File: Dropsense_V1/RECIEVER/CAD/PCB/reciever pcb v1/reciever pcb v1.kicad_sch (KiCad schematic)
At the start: 27 parts, among them J1 1.8inch TFT connector, J2 USB_B_Micro, J3 Battery connector, SW1 EN SW, SW2 IO0 SW, U1 ESP32-S3-WROOM-1, U2 TP4056-42-ESOP8, U3 ME6211C10M5

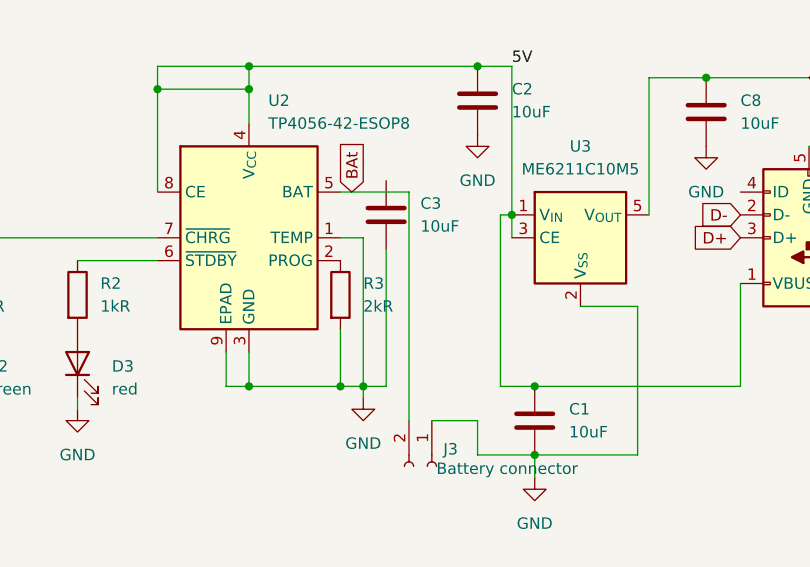
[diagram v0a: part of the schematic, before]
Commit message: Routed and finished reciever pcb
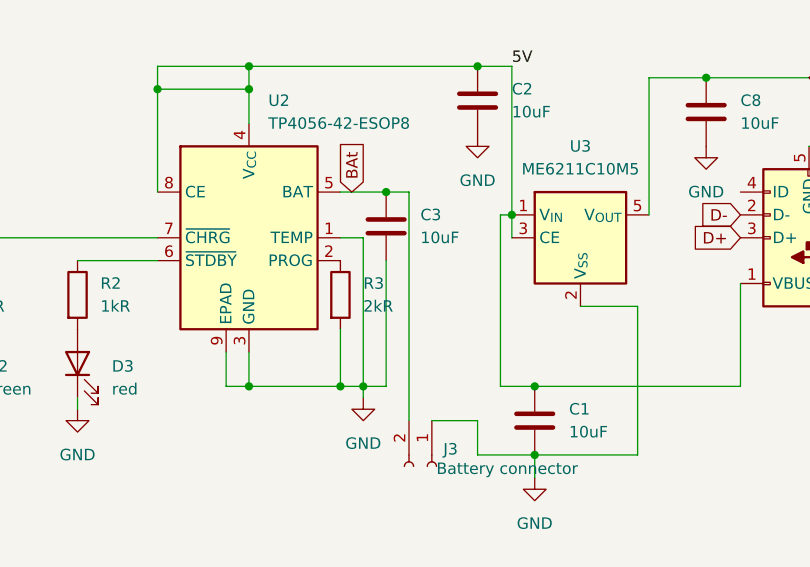
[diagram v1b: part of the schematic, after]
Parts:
- C1, C2, C3, C4, C5, C6, C7, C8: footprint (none) -> Capacitor_SMD:C_0805_2012Metric
- D2, D3: footprint (none) -> LED_SMD:LED_0805_2012Metric
- J1: footprint (none) -> Connector_PinSocket_2.54mm:PinSocket_1x08_P2.54mm_Vertical
- J2: footprint (none) -> Connector_USB:USB_Micro-B_Technik_TWP-4002D-H3
- J3: footprint (none) -> Connector_JST:JST_XH_S2B-XH-A_1x02_P2.50mm_Horizontal
- R1, R2, R3, R4, R5, R6, R7, R8, R9: footprint (none) -> Resistor_SMD:R_0805_2012Metric
- SW1, SW2: footprint (none) -> Button_Switch_THT:SW_PUSH_6mm_H4.3mm
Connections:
- net BAt: now also C3.1
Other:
- moved on the sheet: C3
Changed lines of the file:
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@@
 	)
 	(junction
+		(at 198.12 46.99)
+		(diameter 0)
+		(color 0 0 0 0)
+	)
+	(junction
 		(at 30.48 16.51)
 		(diameter 0)
@@
 	(wire
 		(pts
-			(xy 198.12 53.34) (xy 198.12 68.58)
+			(xy 198.12 54.61) (xy 198.12 68.58)
 		)
 		(stroke
@@
 	(wire
 		(pts
+			(xy 198.12 46.99) (xy 193.04 46.99)
+		)
+		(stroke
+			(width 0)
+			(type default)
+		)
+	)
+	(wire
+		(pts
 			(xy 172.72 35.56) (xy 172.72 46.99)
 		)
@@
 	(wire
 		(pts
-			(xy 200.66 46.99) (xy 193.04 46.99)
+			(xy 200.66 46.99) (xy 198.12 46.99)
 		)
 		(stroke
@@
 			)
 		)
-		(property "Footprint" ""
+		(property "Footprint" "Capacitor_SMD:C_0805_2012Metric"
 			(at 26.3652 24.13 0)
 			(effects
@@
 			)
 		)
-		(property "Footprint" ""
+		(property "Footprint" "Button_Switch_THT:SW_PUSH_6mm_H4.3mm"
 			(at 78.74 142.24 0)
 			(effects
@@
 			)
 		)
-		(property "Footprint" ""
+		(property "Footprint" "Resistor_SMD:R_0805_2012Metric"
 			(at 40.64 133.858 90)
 			(effects
@@
 			)
 		)
-		(property "Footprint" ""
+		(property "Footprint" "Resistor_SMD:R_0805_2012Metric"
 			(at 148.082 58.42 90)
 			(effects
@@
 			)
 		)
-		(property "Footprint" ""
+		(property "Footprint" "Connector_USB:USB_Micro-B_Technik_TWP-4002D-H3"
 			(at 241.3 50.8 0)
 			(effects
@@
 			)
 		)
-		(property "Footprint" ""
+		(property "Footprint" "Capacitor_SMD:C_0805_2012Metric"
 			(at 31.4452 24.13 0)
 			(effects
@@
 			)
 		)
-		(property "Footprint" ""
+		(property "Footprint" "Resistor_SMD:R_0805_2012Metric"
 			(at 28.448 49.53 90)
 			(effects
@@
 			)
 		)
-		(property "Footprint" ""
+		(property "Footprint" "Resistor_SMD:R_0805_2012Metric"
 			(at 173.99 113.538 90)
 			(effects
@@
 			)
 		)
-		(property "Footprint" ""
+		(property "Footprint" "Connector_PinSocket_2.54mm:PinSocket_1x08_P2.54mm_Vertical"
 			(at 93.98 48.26 0)
 			(effects
@@
 			)
 		)
-		(property "Footprint" ""
+		(property "Footprint" "Resistor_SMD:R_0805_2012Metric"
 			(at 80.01 133.858 90)
 			(effects
@@
 			)
 		)
-		(property "Footprint" ""
+		(property "Footprint" "Resistor_SMD:R_0805_2012Metric"
 			(at 191.262 58.42 90)
 			(effects
@@
 			)
 		)
-		(property "Footprint" ""
+		(property "Footprint" "Capacitor_SMD:C_0805_2012Metric"
 			(at 33.9852 154.94 0)
 			(effects
@@
 			)
 		)
-		(property "Footprint" ""
+		(property "Footprint" "LED_SMD:LED_0805_2012Metric"
 			(at 149.86 66.04 0)
 			(effects
@@
 			)
 		)
-		(property "Footprint" ""
+		(property "Footprint" "Resistor_SMD:R_0805_2012Metric"
 			(at 154.94 113.538 90)
 			(effects
@@
 			)
 		)
-		(property "Footprint" ""
+		(property "Footprint" "LED_SMD:LED_0805_2012Metric"
 			(at 163.83 66.04 0)
 			(effects
@@
 			)
 		)
-		(property "Footprint" ""
+		(property "Footprint" "Connector_JST:JST_XH_S2B-XH-A_1x02_P2.50mm_Horizontal"
 			(at 203.2 77.47 0)
 			(effects
@@
 			)
 		)
-		(property "Footprint" ""
+		(property "Footprint" "Capacitor_SMD:C_0805_2012Metric"
 			(at 209.2452 40.64 0)
 			(effects
@@
 			)
 		)
-		(property "Footprint" ""
+		(property "Footprint" "Button_Switch_THT:SW_PUSH_6mm_H4.3mm"
 			(at 27.94 139.7 0)
 			(effects
@@
 			)
 		)
-		(property "Footprint" ""
+		(property "Footprint" "Capacitor_SMD:C_0805_2012Metric"
 			(at 215.5952 76.2 0)
 			(effects
@@
 			)
 		)
-		(property "Footprint" ""
+		(property "Footprint" "Capacitor_SMD:C_0805_2012Metric"
 			(at 37.7952 24.13 0)
 			(effects
@@
 			)
 		)
-		(property "Footprint" ""
+		(property "Footprint" "Capacitor_SMD:C_0805_2012Metric"
 			(at 234.6452 41.91 0)
 			(effects
@@
 			)
 		)
-		(property "Footprint" ""
+		(property "Footprint" "Resistor_SMD:R_0805_2012Metric"
 			(at 62.23 15.748 90)
 			(effects
@@
 			)
 		)
-		(property "Footprint" ""
+		(property "Footprint" "Resistor_SMD:R_0805_2012Metric"
 			(at 162.052 58.42 90)
 			(effects
@@
 	(symbol
 		(lib_id "Device:C")
-		(at 198.12 49.53 0)
+		(at 198.12 50.8 0)
 		(unit 1)
 		(exclude_from_sim no)
@@
 		(fields_autoplaced yes)
 		(property "Reference" "C3"
-			(at 201.93 48.2599 0)
+			(at 201.93 49.5299 0)
 			(effects
 				(font
@@
 		)
 		(property "Value" "10uF"
-			(at 201.93 50.7999 0)
+			(at 201.93 52.0699 0)
 			(effects
 				(font
@@
 			)
 		)
-		(property "Footprint" ""
-			(at 199.0852 53.34 0)
+		(property "Footprint" "Capacitor_SMD:C_0805_2012Metric"
+			(at 199.0852 54.61 0)
 			(effects
 				(font
@@
 		)
 		(property "Datasheet" "~"
-			(at 198.12 49.53 0)
+			(at 198.12 50.8 0)
 			(effects
 				(font
@@
 		)
 		(property "Description" "Unpolarized capacitor"
-			(at 198.12 49.53 0)
+			(at 198.12 50.8 0)
 			(effects
 				(font
